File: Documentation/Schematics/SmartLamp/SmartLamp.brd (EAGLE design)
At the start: 78.4 x 50.8 mm, 26 parts, among them IC1 DS3231/SO, J1 POWER_JACKPTH_BREAD, Q1 IRF1404, Q2 IRF1404, Q3 IRF1404, U1 HM-10

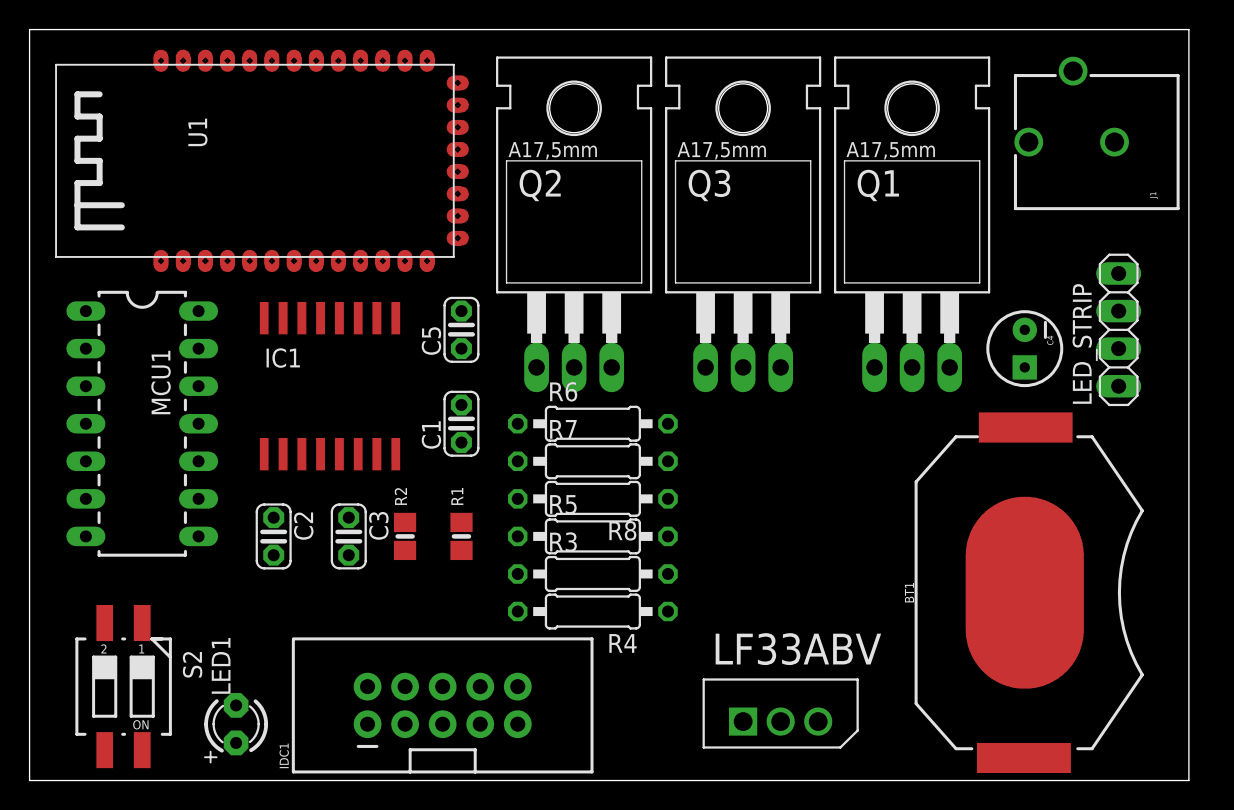
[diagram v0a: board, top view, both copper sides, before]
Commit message: Added datasheets of choosen components, first schematic with BOM
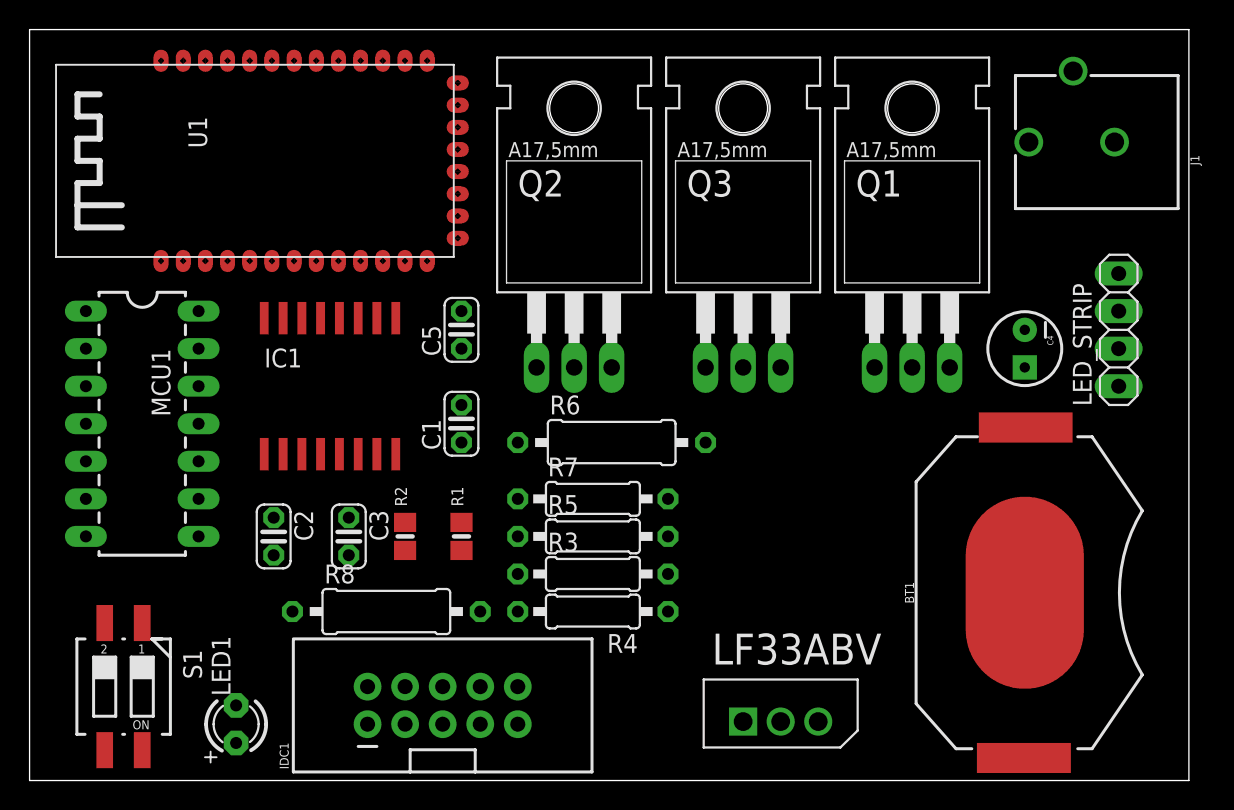
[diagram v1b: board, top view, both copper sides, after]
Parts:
- R3, R4, R5: value 240 -> 220
- R6, R8: device rcl:0207/10 -> rcl:0309/12
- moved R8 15.9 mm to (24.1, 11.4), turned to 0 degrees
- moved R7 2.54 mm to (38.1, 19.1)
- moved R6 1.80 mm to (39.4, 22.9)
- renumbered S2 to S1
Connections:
- removed net N$12: R7.2, U1.23
- removed net VCC: C1.1, C4.1, LF33ABV.3
- new net BLU_KEY: R7.2, S1.2, U1.23
- net +3V3: now also C1.1, C4.1, LF33ABV.3, R7.1, S1.1
- net 3V3: no longer R7.1, S1.1
- net GND: now also S1.3
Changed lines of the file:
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@@
 </class>
 </classes>
-<designrules name="default">
-<description language="de">&lt;b&gt;EAGLE Design Rules&lt;/b&gt;
-&lt;p&gt;
-Die Standard-Design-Rules sind so gewählt, dass sie für
-die meisten Anwendungen passen. Sollte ihre Platine
-besondere Anforderungen haben, treffen Sie die erforderlichen
-Einstellungen hier und speichern die Design Rules unter
-einem neuen Namen ab.</description>
+<designrules name="SparkFun-2-layer">
 <description language="en">&lt;b&gt;EAGLE Design Rules&lt;/b&gt;
 &lt;p&gt;
@@
 <param name="mdViaViaSameLayer" value="8mil"/>
 <param name="mnLayersViaInSmd" value="2"/>
-<param name="mdCopperDimension" value="40mil"/>
+<param name="mdCopperDimension" value="8mil"/>
 <param name="mdDrill" value="8mil"/>
 <param name="mdSmdStop" value="0mil"/>
-<param name="msWidth" value="10mil"/>
-<param name="msDrill" value="24mil"/>
+<param name="msWidth" value="7mil"/>
+<param name="msDrill" value="15mil"/>
 <param name="msMicroVia" value="9.99mm"/>
 <param name="msBlindViaRatio" value="0.5"/>
@@
 <param name="rvMicroViaOuter" value="0.25"/>
 <param name="rvMicroViaInner" value="0.25"/>
-<param name="rlMinPadTop" value="10mil"/>
+<param name="rlMinPadTop" value="12mil"/>
 <param name="rlMaxPadTop" value="20mil"/>
 <param name="rlMinPadInner" value="10mil"/>
 <param name="rlMaxPadInner" value="20mil"/>
-<param name="rlMinPadBottom" value="10mil"/>
+<param name="rlMinPadBottom" value="12mil"/>
 <param name="rlMaxPadBottom" value="20mil"/>
-<param name="rlMinViaOuter" value="8mil"/>
+<param name="rlMinViaOuter" value="10mil"/>
 <param name="rlMaxViaOuter" value="20mil"/>
-<param name="rlMinViaInner" value="8mil"/>
+<param name="rlMinViaInner" value="10mil"/>
 <param name="rlMaxViaInner" value="20mil"/>
 <param name="rlMinMicroViaOuter" value="4mil"/>
@@
 <param name="mlMinCreamFrame" value="0mil"/>
 <param name="mlMaxCreamFrame" value="0mil"/>
-<param name="mlViaStopLimit" value="0mil"/>
+<param name="mlViaStopLimit" value="20mil"/>
 <param name="srRoundness" value="0"/>
 <param name="srMinRoundness" value="0mil"/>
@@
 <param name="dpGapFactor" value="2.5"/>
 <param name="checkGrid" value="0"/>
-<param name="checkAngle" value="0"/>
+<param name="checkAngle" value="1"/>
 <param name="checkFont" value="1"/>
 <param name="checkRestrict" value="1"/>
@@
 <element name="R1" library="microbuilder" package="0805-NO" value="10K" x="29.21" y="16.51" rot="R90"/>
 <element name="R2" library="microbuilder" package="0805-NO" value="10K" x="25.4" y="16.51" rot="R90"/>
-<element name="R6" library="rcl" package="0207/10" value="10K" x="38.1" y="24.13"/>
-<element name="R7" library="rcl" package="0207/10" value="1K" x="38.1" y="21.59"/>
-<element name="R8" library="rcl" package="0207/10" value="470" x="38.1" y="19.05" rot="R180"/>
+<element name="R6" library="rcl" package="0309/12" value="10K" x="39.37" y="22.86"/>
+<element name="R7" library="rcl" package="0207/10" value="1K" x="38.1" y="19.05"/>
+<element name="R8" library="rcl" package="0309/12" value="470" x="24.13" y="11.43"/>
 <element name="U1" library="HM-10_BLE" package="HM-10" value="HM-10" x="15.24" y="41.91" rot="R90"/>
 <element name="Q1" library="transistor-power" package="TO220BH" value="IRF1404" x="59.69" y="34.29"/>
@@
 <element name="Q3" library="transistor-power" package="TO220BH" value="IRF1404" x="48.26" y="34.29"/>
 <element name="LED_STRIP" library="pinhead" package="1X04" value="" x="73.66" y="30.48" rot="R90"/>
-<element name="R3" library="rcl" package="0207/10" value="240" x="38.1" y="13.97"/>
-<element name="R4" library="rcl" package="0207/10" value="240" x="38.1" y="11.43" rot="R180"/>
-<element name="R5" library="rcl" package="0207/10" value="240" x="38.1" y="16.51"/>
+<element name="R3" library="rcl" package="0207/10" value="220" x="38.1" y="13.97"/>
+<element name="R4" library="rcl" package="0207/10" value="220" x="38.1" y="11.43" rot="R180"/>
+<element name="R5" library="rcl" package="0207/10" value="220" x="38.1" y="16.51"/>
 <element name="IDC1" library="SparkFun-Connectors" package="2X5-SHROUDED" value="IDC1" x="27.94" y="5.08" rot="R90">
 <attribute name="PROD_ID" value="CONN-08671" x="27.94" y="5.08" size="1.778" layer="27" rot="R90" display="off"/>
@@
 <attribute name="SF_SKU" value="PRT-11892" x="67.31" y="12.7" size="1.778" layer="27" rot="R90" display="off"/>
 </element>
-<element name="S2" library="switch-dil" package="CTS-219-02" value="219-02" x="6.35" y="6.35" rot="R180">
+<element name="S1" library="switch-dil" package="CTS-219-02" value="219-02" x="6.35" y="6.35" rot="R180">
 <attribute name="MPN" value="" x="6.35" y="6.35" size="1.778" layer="27" rot="R180" display="off"/>
 <attribute name="OC_FARNELL" value="unknown" x="6.35" y="6.35" size="1.778" layer="27" rot="R180" display="off"/>
@@
 <contactref element="IC1" pad="6"/>
 <contactref element="IC1" pad="5"/>
-<contactref element="C2" pad="2"/>
-<contactref element="MCU1" pad="14"/>
 <contactref element="U1" pad="13"/>
 <contactref element="U1" pad="14"/>
@@
 <contactref element="IDC1" pad="10"/>
 <contactref element="BT1" pad="NEGATIVE"/>
+<contactref element="C2" pad="2"/>
+<contactref element="MCU1" pad="14"/>
+<contactref element="S1" pad="3"/>
 <wire x1="67.31" y1="30.48" x2="73.38" y2="43.18" width="0" layer="19" extent="1-1"/>
 <wire x1="62.23" y1="27.94" x2="67.31" y2="30.48" width="0" layer="19" extent="1-1"/>
@@
 <wire x1="11.43" y1="31.75" x2="19.685" y2="31.27" width="0" layer="19" extent="1-1"/>
 <wire x1="13.97" y1="5.08" x2="16.51" y2="15.24" width="0" layer="19" extent="1-1"/>
+<wire x1="5.08" y1="2.05" x2="13.97" y2="5.08" width="0" layer="19" extent="1-1"/>
 <wire x1="28.96" y1="47.18" x2="28.96" y2="36.68" width="0" layer="19" extent="1-1"/>
 <wire x1="26.89" y1="48.68" x2="28.96" y2="47.18" width="0" layer="19" extent="1-1"/>
@@
 <contactref element="C2" pad="1"/>
 <contactref element="MCU1" pad="1"/>
-<contactref element="R7" pad="1"/>
 <contactref element="IDC1" pad="2"/>
-<contactref element="S2" pad="1"/>
-<wire x1="16.51" y1="17.78" x2="33.02" y2="21.59" width="0" layer="19" extent="1-1"/>
-<wire x1="7.62" y1="10.65" x2="16.51" y2="17.78" width="0" layer="19" extent="1-1"/>
 <wire x1="22.86" y1="6.35" x2="16.51" y2="17.78" width="0" layer="19" extent="1-1"/>
 <wire x1="3.81" y1="31.75" x2="16.51" y2="17.78" width="0" layer="19" extent="1-1"/>
@@
 <contactref element="R6" pad="2"/>
 <contactref element="IDC1" pad="5"/>
-<wire x1="27.94" y1="3.81" x2="43.18" y2="24.13" width="0" layer="19" extent="1-1"/>
+<wire x1="27.94" y1="3.81" x2="45.72" y2="22.86" width="0" layer="19" extent="1-1"/>
 <wire x1="3.81" y1="24.13" x2="27.94" y2="3.81" width="0" layer="19" extent="1-1"/>
 </signal>
@@
 <contactref element="U1" pad="24"/>
 <contactref element="R8" pad="2"/>
-<wire x1="33.02" y1="19.05" x2="23.89" y2="48.68" width="0" layer="19" extent="1-1"/>
+<wire x1="30.48" y1="11.43" x2="23.89" y2="48.68" width="0" layer="19" extent="1-1"/>
 </signal>
 <signal name="N$10">
 <contactref element="R8" pad="1"/>
 <contactref element="LED1" pad="A"/>
-<wire x1="13.97" y1="2.54" x2="43.18" y2="19.05" width="0" layer="19" extent="1-1"/>
-</signal>
-<signal name="N$12">
+<wire x1="13.97" y1="2.54" x2="17.78" y2="11.43" width="0" layer="19" extent="1-1"/>
+</signal>
+<signal name="BLU_KEY">
 <contactref element="U1" pad="23"/>
 <contactref element="R7" pad="2"/>
-<wire x1="43.18" y1="21.59" x2="25.39" y2="48.68" width="0" layer="19" extent="1-1"/>
+<contactref element="S1" pad="2"/>
+<wire x1="43.18" y1="19.05" x2="25.39" y2="48.68" width="0" layer="19" extent="1-1"/>
+<wire x1="5.08" y1="10.65" x2="43.18" y2="19.05" width="0" layer="19" extent="1-1"/>
 </signal>
 <signal name="N$3" class="1">
@@
 </signal>
 <signal name="N$2">
-<contactref element="S2" pad="4"/>
+<contactref element="S1" pad="4"/>
 <contactref element="C5" pad="1"/>
 <wire x1="7.62" y1="2.05" x2="29.21" y2="29.21" width="0" layer="19" extent="1-1"/>
-</signal>
-<signal name="VCC" class="1">
-<contactref element="LF33ABV" pad="3"/>
-<contactref element="C4" pad="1"/>
-<contactref element="C1" pad="1"/>
-<wire x1="53.34" y1="3.9878" x2="67.31" y2="27.94" width="0" layer="19" extent="1-1"/>
-<wire x1="29.21" y1="22.86" x2="53.34" y2="3.9878" width="0" layer="19" extent="1-1"/>
 </signal>
 <signal name="+3V3" class="2">
@@
 <contactref element="R2" pad="1"/>
 <contactref element="R1" pad="1"/>
-<wire x1="29.21" y1="15.56" x2="33.02" y2="24.13" width="0" layer="19" extent="1-1"/>
+<contactref element="LF33ABV" pad="3"/>
+<contactref element="C4" pad="1"/>
+<contactref element="C1" pad="1"/>
+<contactref element="R7" pad="1"/>
+<contactref element="S1" pad="1"/>
+<wire x1="53.34" y1="3.9878" x2="67.31" y2="27.94" width="0" layer="19" extent="1-1"/>
+<wire x1="33.02" y1="19.05" x2="53.34" y2="3.9878" width="0" layer="19" extent="1-1"/>
+<wire x1="33.02" y1="22.86" x2="33.02" y2="19.05" width="0" layer="19" extent="1-1"/>
+<wire x1="29.21" y1="22.86" x2="33.02" y2="22.86" width="0" layer="19" extent="1-1"/>
+<wire x1="29.21" y1="15.56" x2="33.02" y2="19.05" width="0" layer="19" extent="1-1"/>
 <wire x1="25.4" y1="15.56" x2="29.21" y2="15.56" width="0" layer="19" extent="1-1"/>
 <wire x1="21.59" y1="17.78" x2="25.4" y2="15.56" width="0" layer="19" extent="1-1"/>
 <wire x1="17.145" y1="22.07" x2="21.59" y2="17.78" width="0" layer="19" extent="1-1"/>
+<wire x1="7.62" y1="10.65" x2="17.145" y2="22.07" width="0" layer="19" extent="1-1"/>
 </signal>
 </signals>
